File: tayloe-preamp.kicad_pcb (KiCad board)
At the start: 2 copper layers, 39 x 21 mm, 13 parts, among them J1 PCB_SMA_EDGE, J2 PCB_SMA_EDGE, J3 Conn_01x01_Female, Q1 2N2222, T1 T37_XFRM

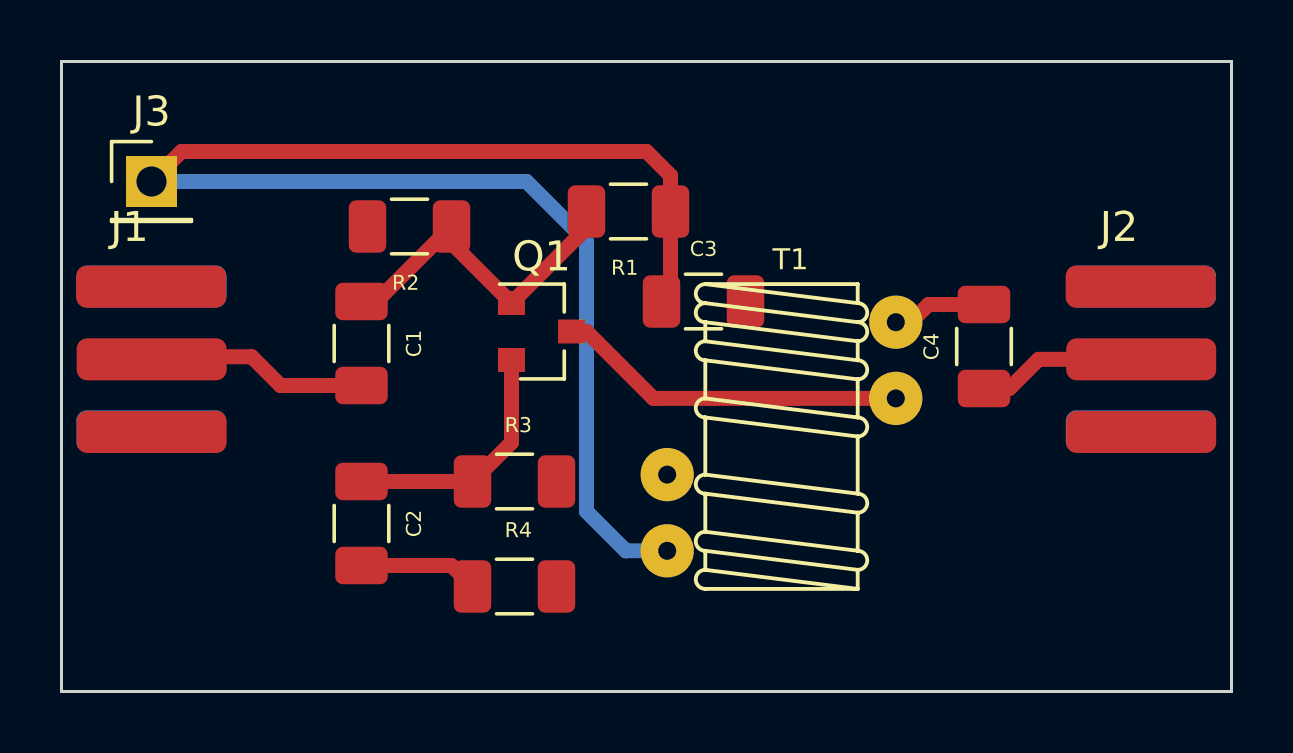
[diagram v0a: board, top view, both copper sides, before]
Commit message: added 50 ohm input
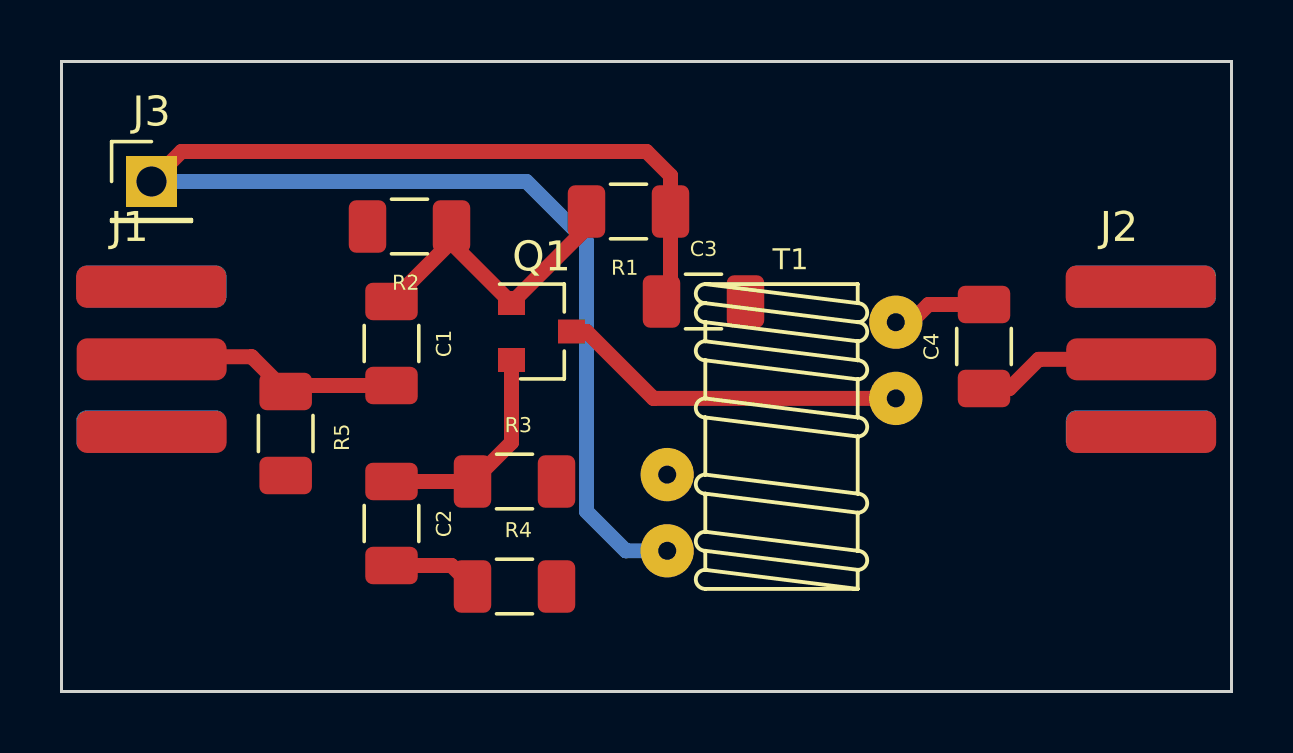
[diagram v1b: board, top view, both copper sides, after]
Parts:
- added R5: 50, Xenir:Resistor 1206, F.Cu at (153.8, 95.5)
- R3: value 100 -> 50
- R4: value 200 -> 68
- moved C1 1.00 mm to (157.2, 92.4)
- moved C2 1.00 mm to (157.2, 98.4)
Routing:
- net Net-(C2-Pad1): track 8.29 -> 7.29 mm
- net Net-(C2-Pad2): track 3.99 -> 2.99 mm
- net Net-(C1-Pad2): track 7.39 -> 8.39 mm
- net Net-(C1-Pad1): track 11.5 -> 10.8 mm
